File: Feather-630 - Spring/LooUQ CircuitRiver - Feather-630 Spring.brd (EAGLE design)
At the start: 102.5 x 70.7 mm, 23 parts, among them J1 FEATHERHOST-S, J2 FEATHERHOST-L, J3 CR-SPRING HEADER, J4 JST PH-2 T/H, J5 JST PH-2 T/H, J6 QWIIC VERTICAL, J7 B8B-PH-K-S(LF)(SN), J8 DNF, P3 BREAKOUTPAD, U2 LM2674 BUCK

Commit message: Updates for Feather-630
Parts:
- P3: value BREAKOUTPAD -> DNF
- moved C4 13.9 mm to (42.4, 48.3), turned to 0 degrees
- moved R2 13.8 mm to (39.8, 46.3), turned to 270 degrees
- moved R1 13.3 mm to (37.1, 48.3), turned to 180 degrees
- moved P3 11.9 mm to (45.6, 5.40)
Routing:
- net Net_8: track 43.7 -> 66.1 mm
- net Net_7: track 36.2 -> 54.9 mm, vias 1 -> 2
- net Net_5: track 50.3 -> 66.5 mm, vias 1 -> 2
- net Net_GND: track 34.1 -> 21.0 mm
- net Net_22: track 10.1 -> 21.6 mm
- net Net_19: track 68.3 -> 60.1 mm, vias 0 -> 2
- net Net_18: track 26.3 -> 18.6 mm
- net Net_2: track 80.2 -> 72.8 mm
- net Net_6: track 80.4 -> 76.0 mm, vias 0 -> 2
- net Net_4: track 69.4 -> 73.6 mm
- net Net_VIn: track 40.2 -> 44.2 mm
- net Net_9: track 61.9 -> 65.8 mm, vias 0 -> 2
- net Net_28: track 43.8 -> 40.1 mm
- net Net_27: track 46.6 -> 43.0 mm
- net Net_1: track 73.3 -> 76.3 mm
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- added copper zone on layer 1, net Net_1
- added copper zone on layer 1, net Net_12
- added copper zone on layer 1, net Net_14
- added copper zone on layer 1, net Net_18
- added copper zone on layer 1, net Net_19
- added copper zone on layer 1, net Net_26
- added copper zone on layer 1, net Net_4
- added copper zone on layer 1, net Net_5
- added copper zone on layer 1, net Net_7
- added copper zone on layer 1, net Net_9
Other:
- board text added: "3v3"
- board text added: "Antenna Power"
- board text added: "GND"
- board text added: "GPS Active"
- board text removed: "Feather Short Header"

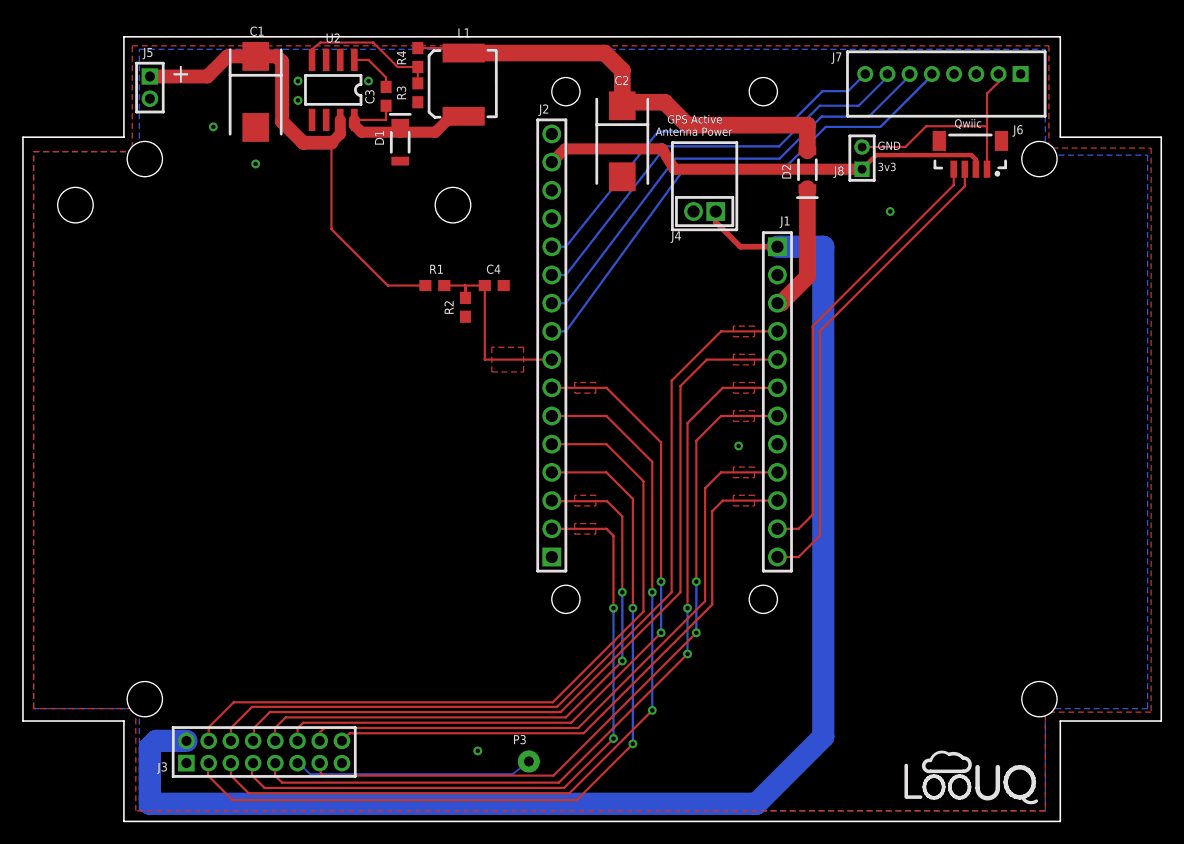
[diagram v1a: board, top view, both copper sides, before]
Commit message: updated with CircuitRiver RapidsIO connector
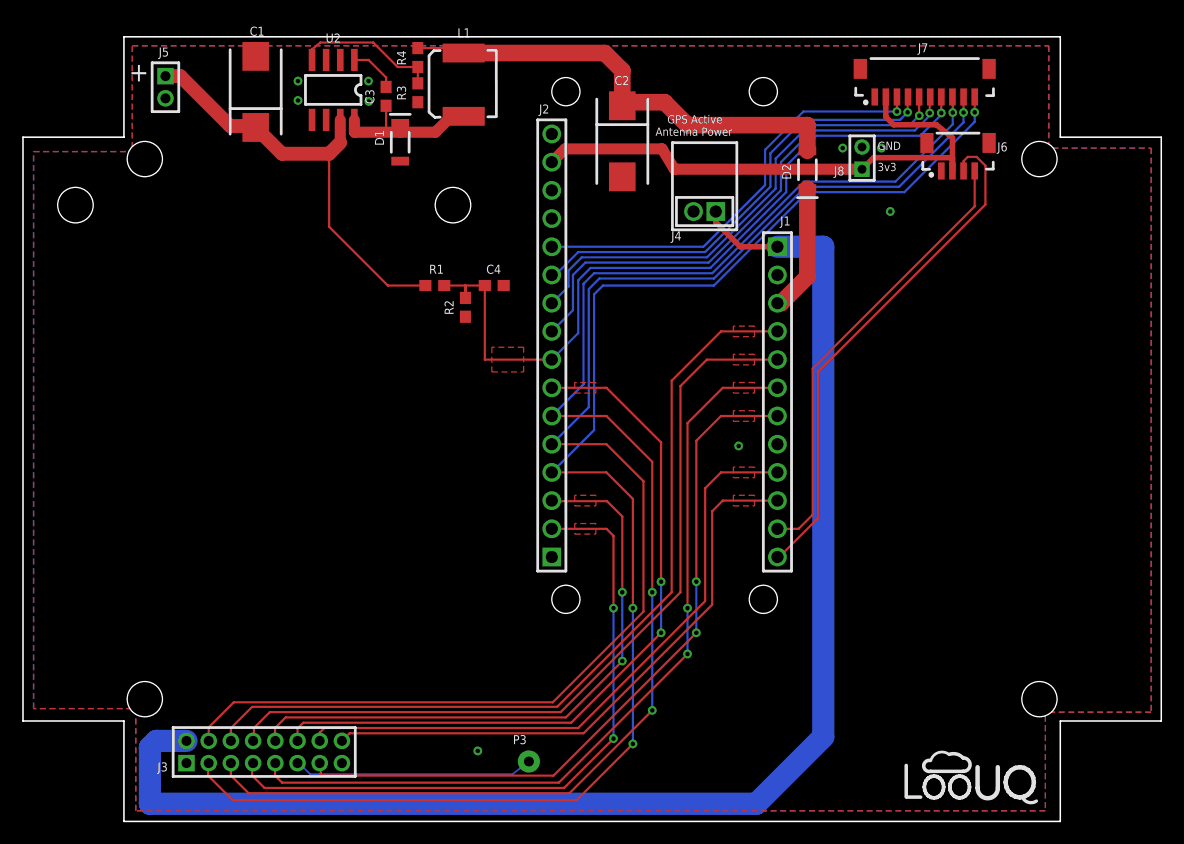
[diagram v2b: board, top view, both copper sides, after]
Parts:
- J6: device common:JST-SH_SMD-TE_Qwiic -> common:JST-SH_SMD-TopEntry_Qwiic
- J7: value B8B-PH-K-S(LF)(SN) -> CR-RAPIDSIO VERTICAL; device common:HDR-1x8T/2/Sh18x6 -> common:JST-SH_SMD-TopEntry_Rapids
- P3: value DNF -> SLEEP
- moved J7 2.64 mm to (81.2, 65.2), turned to 0 degrees
- moved J6 2.36 mm to (84.2, 58.6)
- moved J5 1.40 mm to (12.8, 66.1)
- turned C1 to 90 degrees
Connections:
- net Net_0 renamed Net_VBUS
- net Net_3 renamed Net_VSW
- removed net Net_24: J2.10, J7.6
- removed net Net_29: J2.15, J6.2, J8.1
- new net Net_15: J2.10, J7.5
- new net Net_3v3: J2.15, J6.2, J7.2, J8.1
- net Net_11: now also J7.3; no longer J7.8
- net Net_18: now also J7.7
- net Net_2: now also J7.10
- net Net_23: now also J7.6; no longer J7.5
- net Net_25: now also J7.4; no longer J7.7
- net Net_6: now also J7.8
- net Net_8: now also J7.9
- net Net_GND: now also J7.1; no longer J7.2
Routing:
- net Net_2: track 72.8 -> 133.4 mm, vias 2 -> 3
- net Net_8: track 66.1 -> 123.7 mm, vias 0 -> 1
- net Net_6: track 76.0 -> 130.7 mm, vias 2 -> 3
- net Net_3v3: track 0.00 -> 50.7 mm
- net Net_18: track 18.6 -> 68.6 mm, vias 0 -> 1
- net Net_15: track 0.00 -> 44.2 mm, vias 0 -> 1
- net Net_24: track 42.0 -> 0.00 mm
- net Net_29: track 41.3 -> 0.00 mm
- net Net_GND: track 21.0 -> 0.00 mm, vias 8 -> 7
- net Net_VIn: track 44.2 -> 38.6 mm
- net Net_11: track 35.4 -> 39.3 mm, vias 0 -> 1
- net Net_27: track 43.0 -> 46.4 mm
- net Net_VSW: track 16.1 -> 18.6 mm
- net Net_25: track 39.1 -> 41.3 mm, vias 0 -> 1
- net Net_23: track 45.3 -> 47.2 mm, vias 0 -> 1
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
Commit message: Updated Feathers
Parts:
- added P1, P2: DNF, common:BreakoutConn
- P3: value SLEEP -> DNF
- moved J8 1.24 mm to (74.3, 59.7)
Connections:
- new net Net_29: J2.14, J8.1
- new net Net_30: J2.16, P1.1
- net Net_3v3: now also J8.2; no longer J8.1
- net Net_GND: now also P2.1; no longer J8.2
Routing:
- net Net_30: track 0.00 -> 32.1 mm
- net Net_29: track 0.00 -> 29.0 mm
- net Net_3v3: track 50.7 -> 45.1 mm
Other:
- board text added: "A.Ref"
- board text added: "MCU"
- board text removed: "GND"

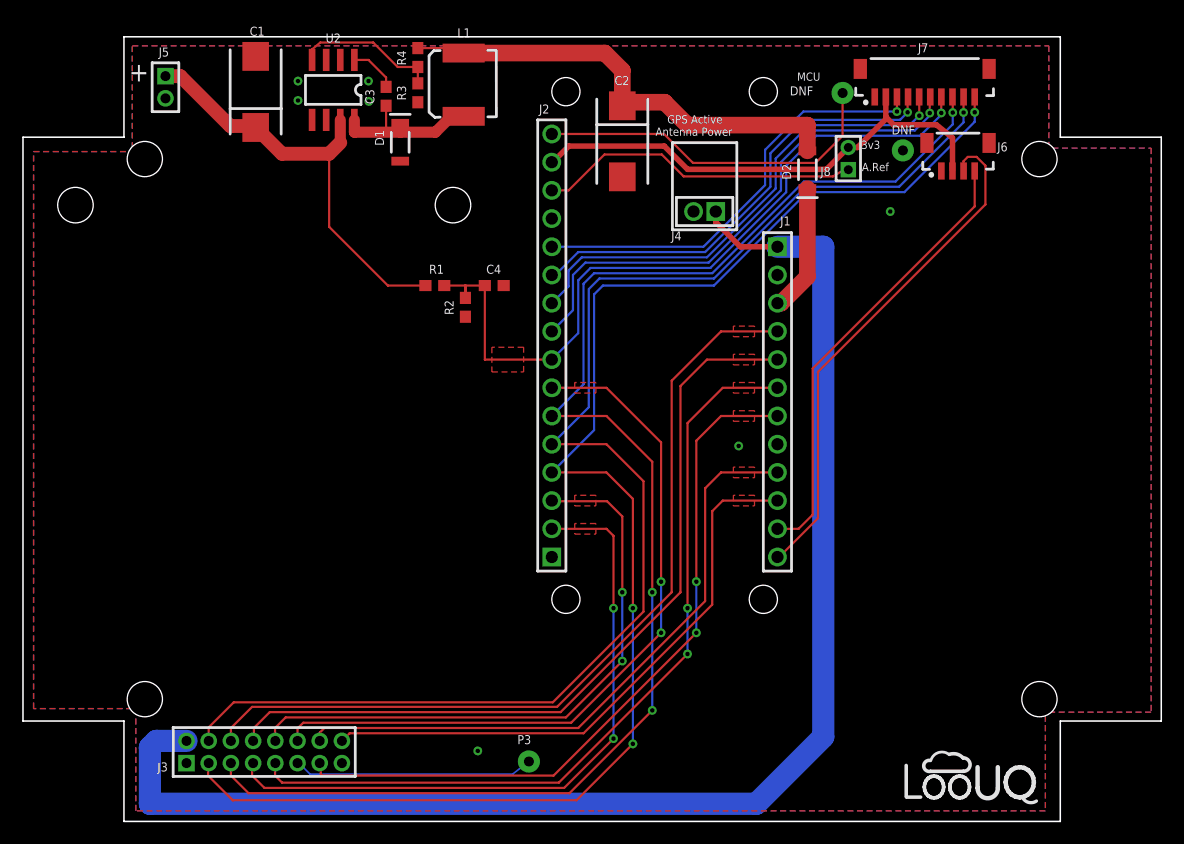
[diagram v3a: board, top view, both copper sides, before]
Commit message: Moved RapidsIO, chg L1 on F-630
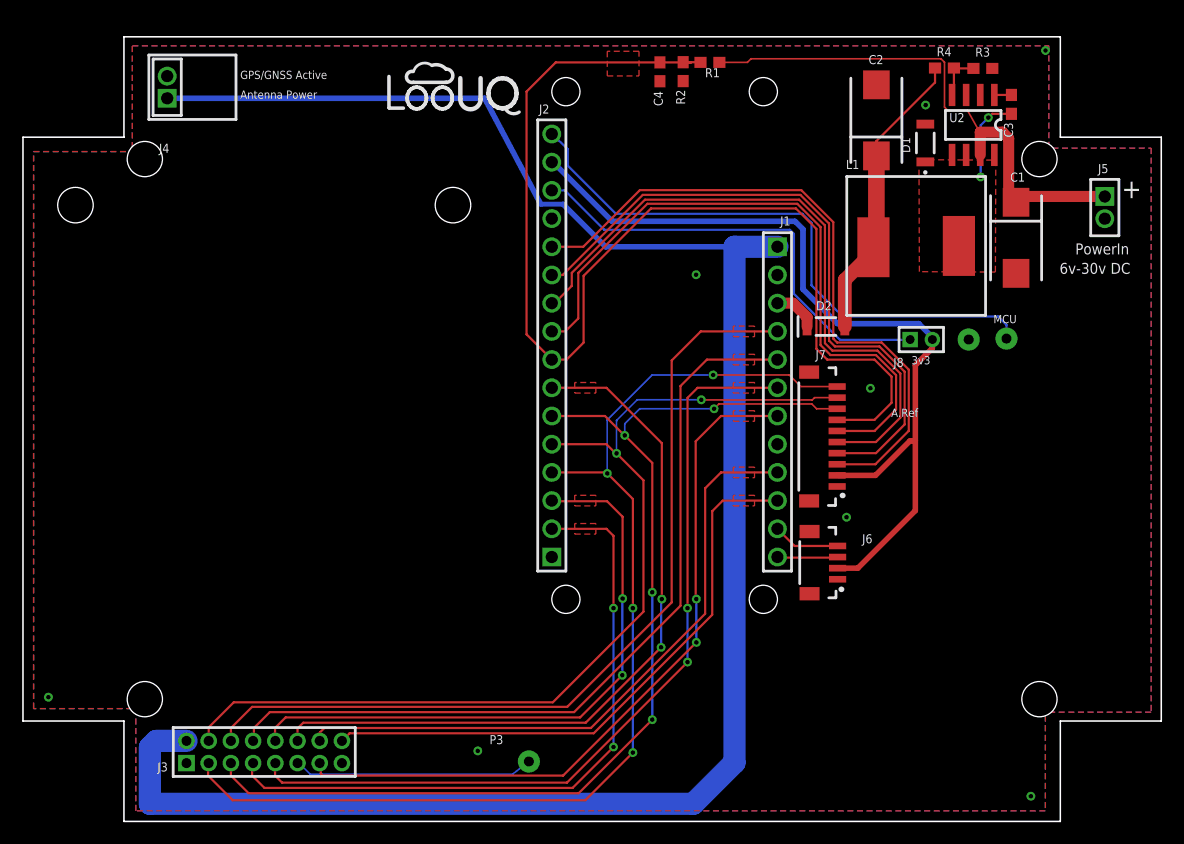
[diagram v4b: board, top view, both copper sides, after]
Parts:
- D2: device common:SOD-123 -> common:SOD-123_D2
- J4: value JST PH-2 T/H -> JST PH-2 R/A T/H; device common:JST_PH-2_T/H -> common:JST_PH-2_R/A_T/H
- J5: value JST PH-2 T/H -> JST PH-2 VERT T/H; device common:HDR-2x1T/2x2/2x4 -> common:JST_PH-2_VERT_T/H
- J6: device common:JST-SH_SMD-TopEntry_Qwiic -> common:JST_SH-04_VERT_SMD_Qwiic
- L1: value 100uH -> 220uH; device common:Panasonic_H-Series_Inductor -> common:Bourns_SRR1260_Series
- LG1: value LOOUQ LOGO -> DNF
- LG2: value CIRCUITRIVER LOGO -> DNF
- moved J5 85.3 mm to (97.4, 55.3)
- moved LG1 77.6 mm to (38.8, 66.0)
- moved C1 69.7 mm to (89.4, 52.6), turned to 270 degrees
- moved U2 57.7 mm to (85.6, 62.7)
- moved C3 56.3 mm to (89.0, 64.6)
- moved R3 50.9 mm to (86.4, 67.8), turned to 180 degrees
- moved J4 49.7 mm to (13.0, 66.1), turned to 0 degrees
- moved R4 47.4 mm to (83.0, 67.8), turned to 180 degrees
- moved D1 47.3 mm to (81.3, 61.1), turned to 90 degrees
- moved L1 43.3 mm to (80.4, 51.8), turned to 180 degrees
- moved J6 36.9 mm to (73.4, 23.3), turned to 90 degrees
- moved R1 31.9 mm to (61.9, 68.4), turned to 0 degrees
- moved J7 31.6 mm to (73.3, 34.7), turned to 90 degrees
- moved R2 28.9 mm to (59.5, 67.5)
- moved P1 26.6 mm to (88.6, 43.5)
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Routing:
- net Net_VBAT: track 127.4 -> 175.4 mm
- net Net_27: track 46.4 -> 5.53 mm
- net Net_18: track 68.6 -> 103.5 mm, vias 1 -> 0
- net Net_28: track 40.7 -> 6.06 mm
- net Net_8: track 123.7 -> 89.9 mm, vias 1 -> 2
- net Net_6: track 130.7 -> 97.5 mm, vias 3 -> 4
- net Net_3v3: track 45.1 -> 77.7 mm
- net Net_2: track 133.4 -> 100.9 mm, vias 3 -> 4
- net Net_30: track 32.1 -> 53.5 mm
- net Net_11: track 39.3 -> 60.3 mm, vias 1 -> 0
- net Net_25: track 41.3 -> 59.4 mm, vias 1 -> 0
- net Net_21: track 42.4 -> 26.6 mm
- net Net_15: track 44.2 -> 59.2 mm, vias 1 -> 0
- net Net_23: track 47.2 -> 60.1 mm, vias 1 -> 0
- net Net_29: track 29.0 -> 41.0 mm
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- added copper zone on layer 1, net Net_VSW
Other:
- board text added: "6v-30v DC"
- board text added: "F.Batt"
- board text added: "Feather-630 Spring v1.6a"
- board text added: "GPS/GNSS Active"
- board text added: "PowerIn"
- board text removed: "F.Pwr"
- board text removed: "Feather-630 Spring v1.6"
- board text removed: "GPS Active"
